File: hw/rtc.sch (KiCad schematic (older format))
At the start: 3 parts

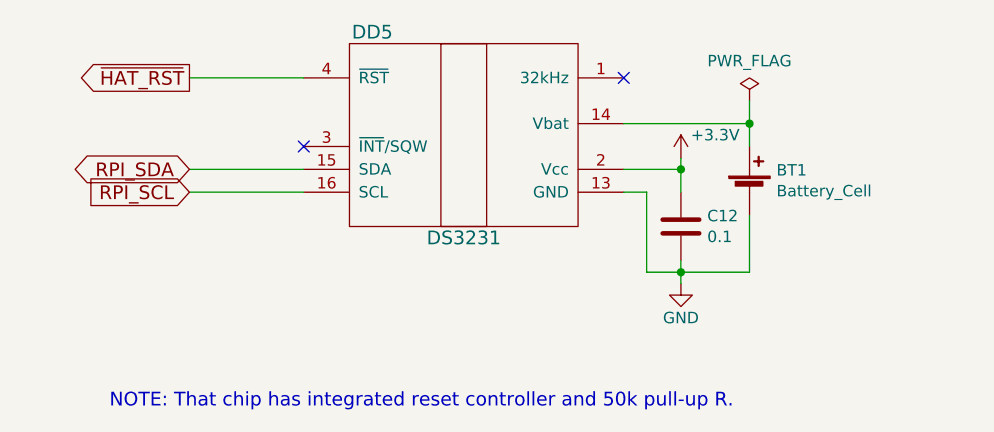
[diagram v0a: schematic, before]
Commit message: hw: cvpcb for R,C
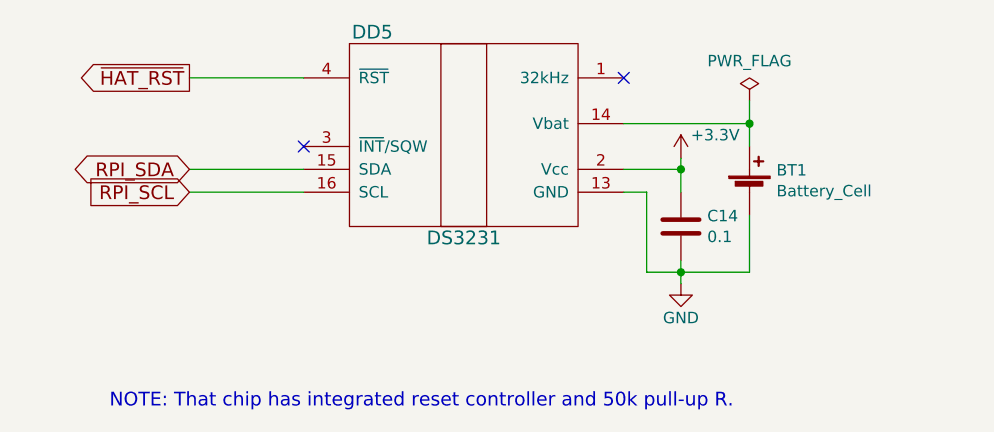
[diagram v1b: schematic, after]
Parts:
- C14: renamed from C12; footprint (none) -> Capacitor_SMD:C_0603_1608Metric
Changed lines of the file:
@@
 $EndComp
 $Comp
-L Device:C C12
+L Device:C C14
 U 1 1 5AC0D763
 P 5350 5400
-F 0 "C12" H 5465 5446 50  0000 L CNN
+F 0 "C14" H 5465 5446 50  0000 L CNN
 F 1 "0.1" H 5465 5355 50  0000 L CNN
-F 2 "" H 5388 5250 50  0001 C CNN
+F 2 "Capacitor_SMD:C_0603_1608Metric" H 5388 5250 50  0001 C CNN
 F 3 "~" H 5350 5400 50  0001 C CNN
 	1    5350 5400
@@
 $EndComp
 $Comp
-L power:PWR_FLAG #FLG0103
+L power:PWR_FLAG #FLG03
 U 1 1 5AE576E6
 P 5650 4850
-F 0 "#FLG0103" H 5650 4925 50  0001 C CNN
+F 0 "#FLG03" H 5650 4925 50  0001 C CNN
 F 1 "PWR_FLAG" H 5650 5024 50  0000 C CNN
 F 2 "" H 5650 4850 50  0001 C CNN

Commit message: hw: wonring on NET
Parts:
- DD5: footprint Housings_SOIC:SOIC-16W_7.5x10.3mm_Pitch1.27mm -> Package_SO:SOIC-16W_7.5x10.3mm_P1.27mm
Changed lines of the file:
@@
 F 0 "DD5" H 4000 5450 60  0000 C CNN
 F 1 "DS3231" H 4400 4550 60  0000 C CNN
-F 2 "Housings_SOIC:SOIC-16W_7.5x10.3mm_Pitch1.27mm" H 4400 5050 60  0001 C CNN
+F 2 "Package_SO:SOIC-16W_7.5x10.3mm_P1.27mm" H 4400 5050 60  0001 C CNN
 F 3 "" H 4400 5050 60  0001 C CNN
 	1    4400 5000

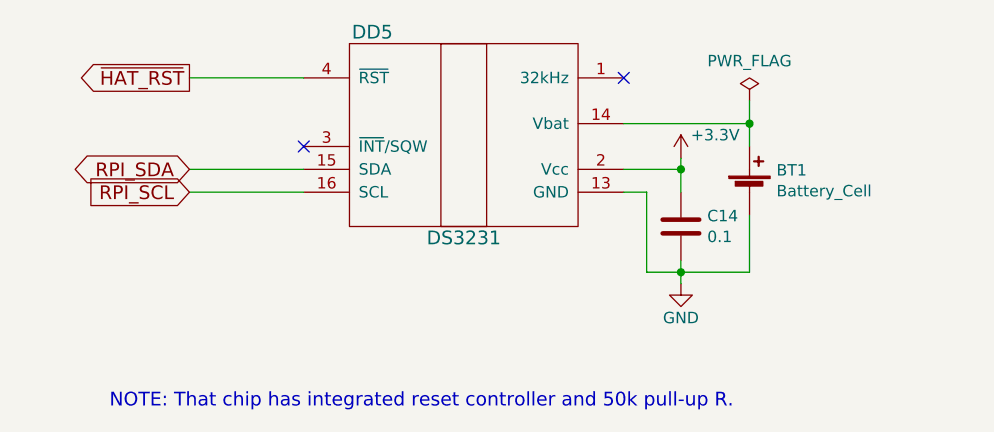
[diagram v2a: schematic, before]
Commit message: hw: connect GH mount points with GND, add 3V battery
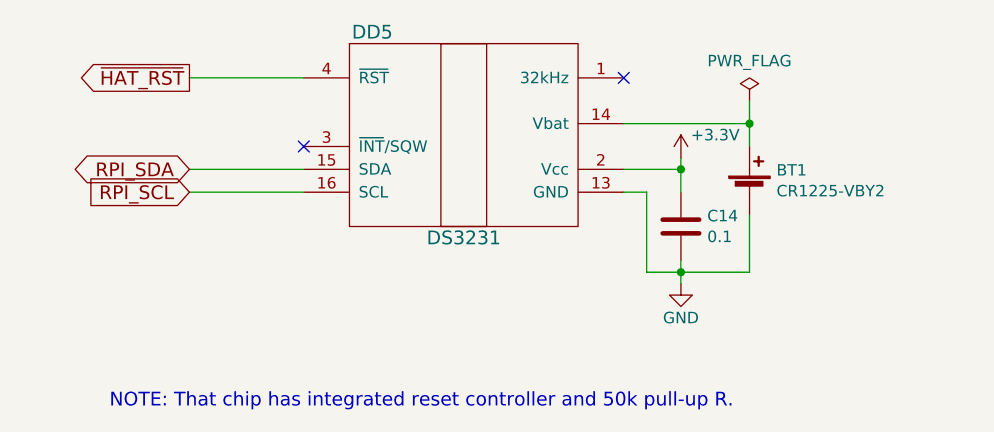
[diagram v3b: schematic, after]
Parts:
- BT1: value Battery_Cell -> CR1225-VBY2; footprint (none) -> hat:CR1225-VBY2
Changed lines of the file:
@@
 P 5650 5250
 F 0 "BT1" H 5768 5346 50  0000 L CNN
-F 1 "Battery_Cell" H 5768 5255 50  0000 L CNN
-F 2 "" V 5650 5310 50  0001 C CNN
+F 1 "CR1225-VBY2" H 5768 5255 50  0000 L CNN
+F 2 "hat:CR1225-VBY2" V 5650 5310 50  0001 C CNN
 F 3 "~" V 5650 5310 50  0001 C CNN
 	1    5650 5250

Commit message: hw: remove header with unused rpi gpio's, more net labels
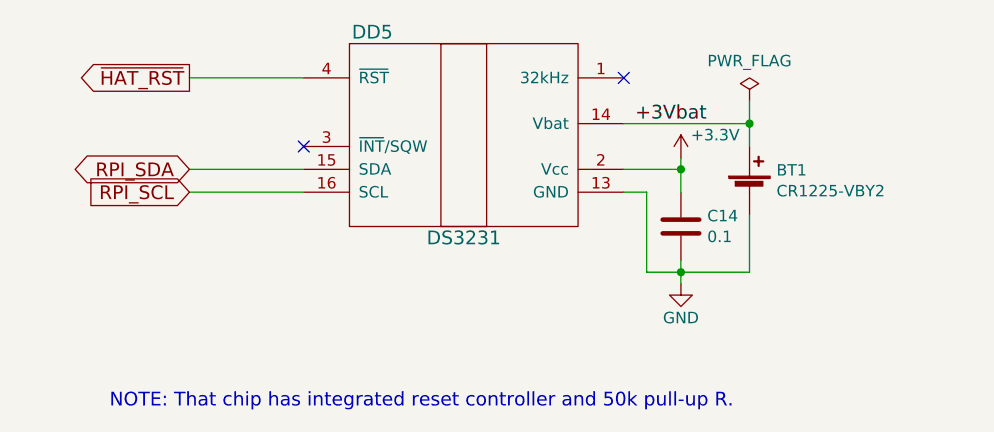
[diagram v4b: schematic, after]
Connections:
- net +3Vbat: now reaches BT1.1 (+), DD5.14 (Vbat)
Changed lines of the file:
@@
 	5650 4850 5650 4950
 Connection ~ 5650 4950
+Text Label 5150 4950 0    60   ~ 0
++3Vbat
 $EndSCHEMATC
